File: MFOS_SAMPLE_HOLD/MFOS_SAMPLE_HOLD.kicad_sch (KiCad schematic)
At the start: 94 parts, among them J1 Jack-DC, J10 Conn_01x01, J11 Conn_01x01, J12 Conn_01x01, J13 Conn_01x01, J14 Conn_01x01, J15 Conn_01x01, J16 Conn_01x01, J17 Conn_01x01, J18 Conn_01x01, J19 Conn_01x01, J2 Jack-DC, J20 Conn_01x01, J3 Jack-DC, J4 Jack-DC, J5 Jack-DC, J6 Jack-DC, J7 Jack-DC, J8 Conn_01x01, J9 Conn_01x01, Q1 2N3904, Q2 2N3904, Q3 2N3904, Q4 J112, Q5 J112, Q6 J112, U1 TL074, U2 TL082, U3 LF444

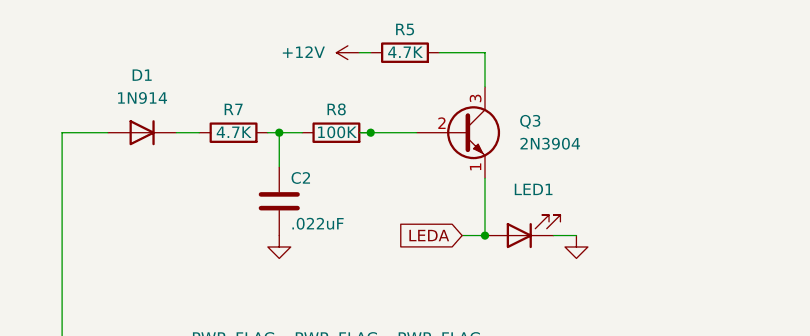
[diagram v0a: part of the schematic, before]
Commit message: Updated BOM, renamed VCO > MFOS_VCO
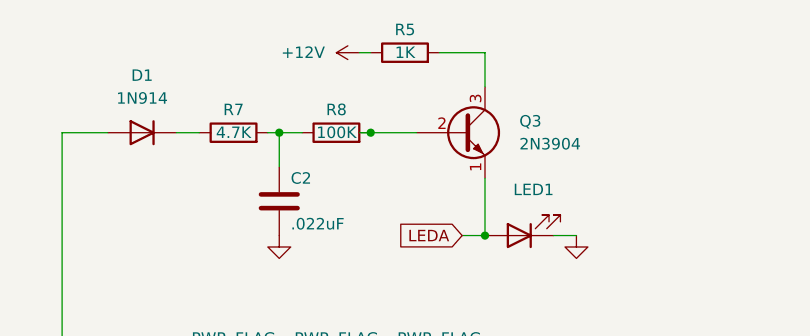
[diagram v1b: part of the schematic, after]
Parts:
- R5: value 4.7K -> 1K
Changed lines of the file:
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@@
     (in_bom yes) (on_board yes)
     (property "Reference" "R5" (id 0) (at 198.12 24.13 90))
-    (property "Value" "4.7K" (id 1) (at 198.12 26.67 90))
+    (property "Value" "1K" (id 1) (at 198.12 26.67 90))
     (property "Footprint" "" (id 2) (at 198.12 28.448 90)
       (effects (font (size 1.27 1.27)) hide)
@@
     )
     (path "/9da687fc-1551-41db-960a-e23aea2daa27"
-      (reference "R5") (unit 1) (value "4.7K") (footprint "")
+      (reference "R5") (unit 1) (value "1K") (footprint "")
     )
     (path "/f7d900a7-907c-49dd-9ace-fc968800f1a3"

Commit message: Reviewed BOM
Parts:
- C17: symbol Device:C -> dhk:C_Polystyrene
- J10, J11, J12, J13, J14, J15, J16, J17, J18, J19, J20, J8, J9: now left out of the parts list

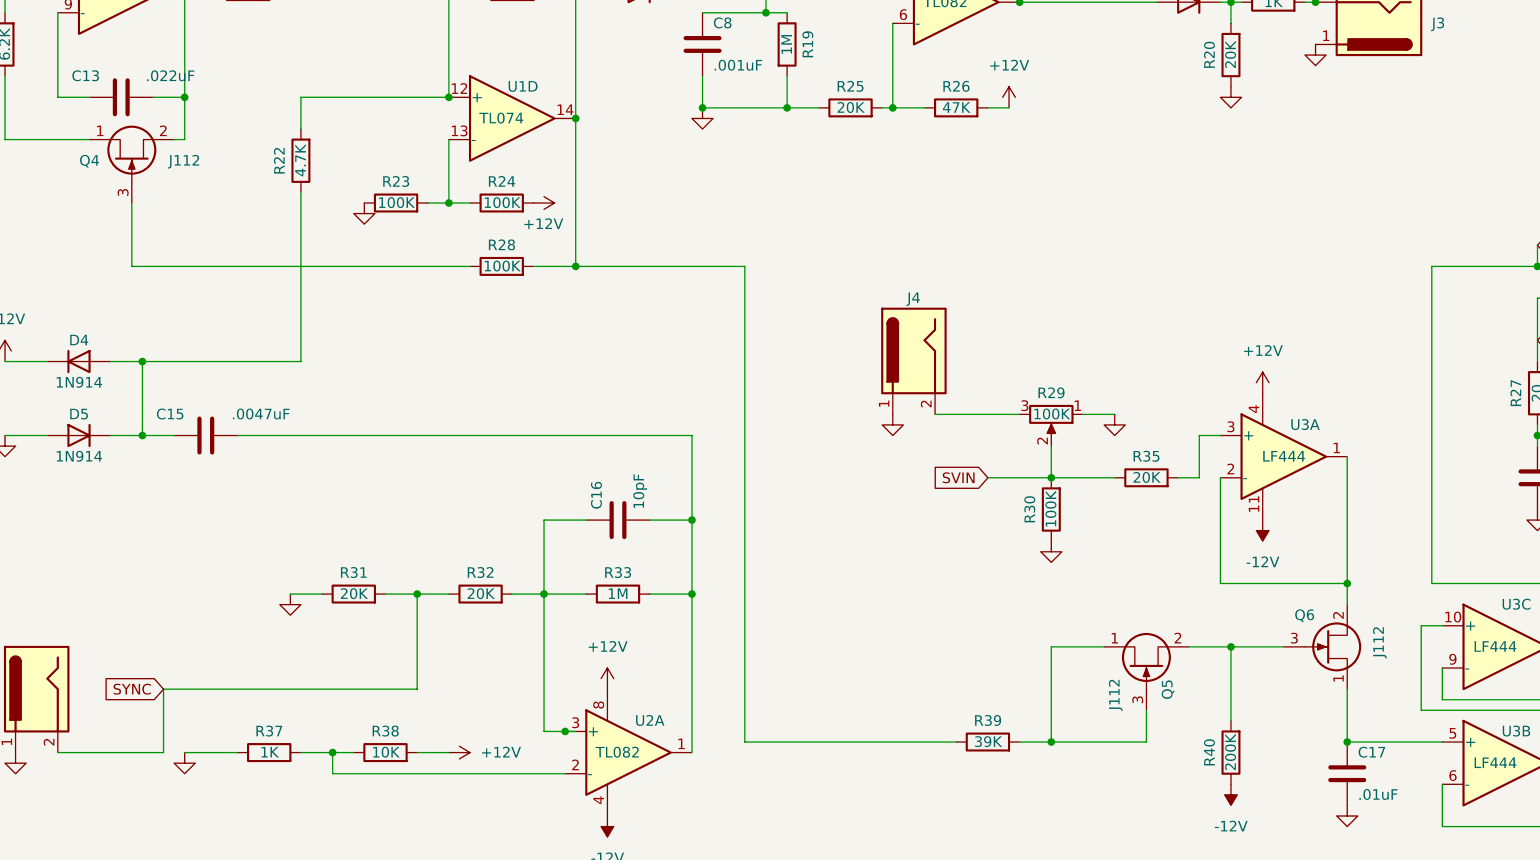
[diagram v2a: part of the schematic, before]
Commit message: Designs adapted for BOM
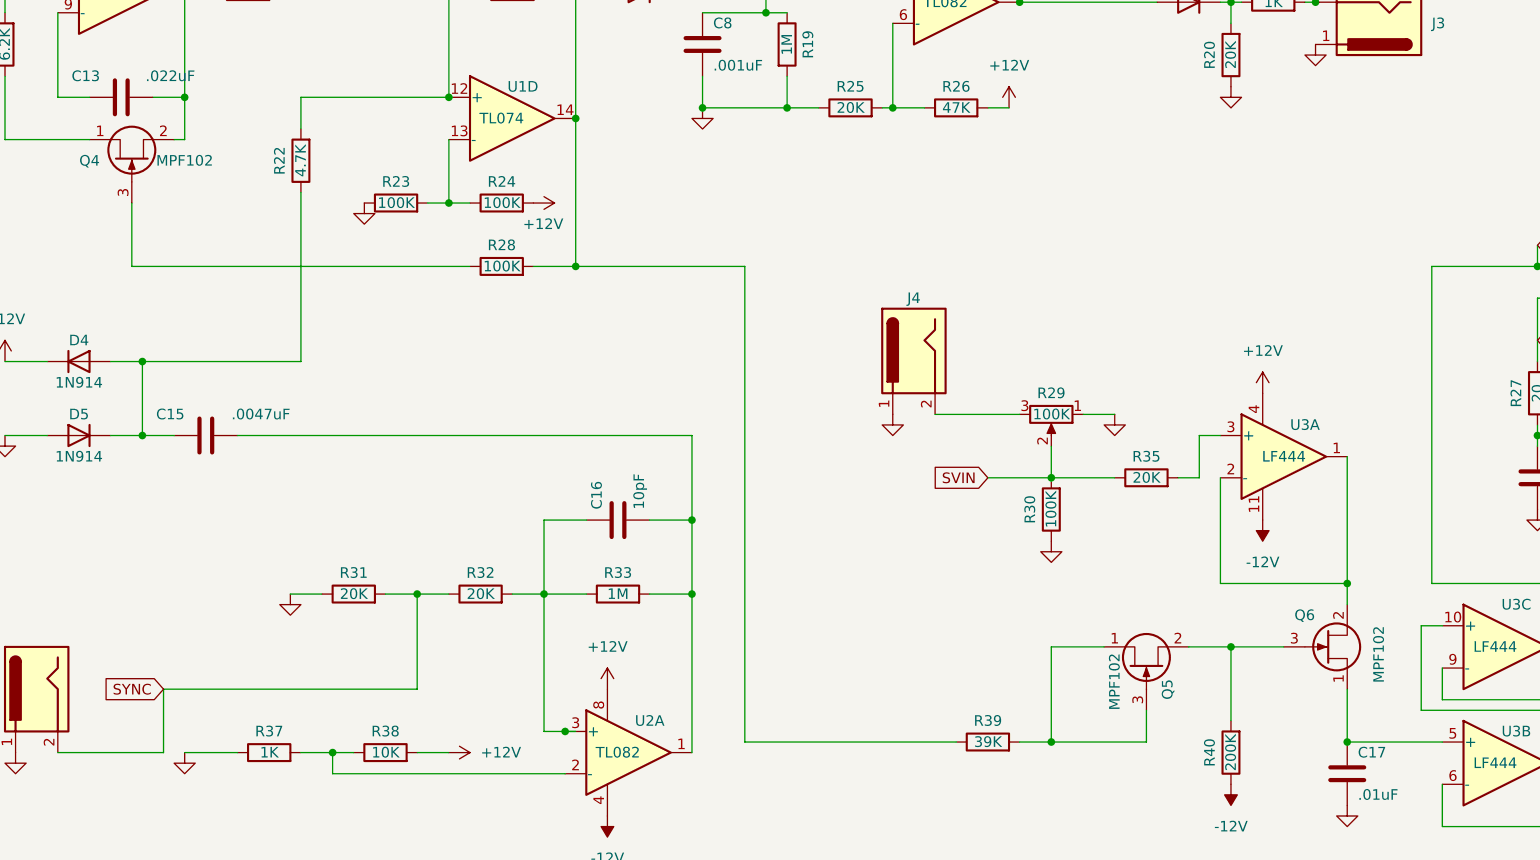
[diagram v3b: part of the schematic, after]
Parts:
- Q4, Q5, Q6: value J112 -> MPF102
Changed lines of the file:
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@@
       (effects (font (size 1.27 1.27)) (justify left))
     )
-    (property "Value" "J112" (id 1) (at 163.83 181.61 0)
+    (property "Value" "MPF102" (id 1) (at 163.83 181.61 0)
       (effects (font (size 1.27 1.27)) (justify left))
     )
@@
     (in_bom yes) (on_board yes)
     (property "Reference" "Q4" (id 0) (at 40.64 115.57 90))
-    (property "Value" "J112" (id 1) (at 52.07 115.57 90))
+    (property "Value" "MPF102" (id 1) (at 52.07 115.57 90))
     (property "Footprint" "" (id 2) (at 47.625 110.49 0)
       (effects (font (size 1.27 1.27) italic) (justify left) hide)
@@
       (effects (font (size 1.27 1.27)) (justify left))
     )
-    (property "Value" "J112" (id 1) (at 195.58 171.45 90)
+    (property "Value" "MPF102" (id 1) (at 195.58 171.45 90)
       (effects (font (size 1.27 1.27)) (justify left))
     )
@@
     )
     (path "/7319e780-225d-49c8-b443-e4647f2dcf5f"
-      (reference "Q4") (unit 1) (value "J112") (footprint "")
+      (reference "Q4") (unit 1) (value "MPF102") (footprint "")
     )
     (path "/411993a9-df9b-475b-acd7-b390e54f2b94"
-      (reference "Q5") (unit 1) (value "J112") (footprint "")
+      (reference "Q5") (unit 1) (value "MPF102") (footprint "")
     )
     (path "/945ed899-8bd2-4078-9704-4e2d00c36e55"
-      (reference "Q6") (unit 1) (value "J112") (footprint "")
+      (reference "Q6") (unit 1) (value "MPF102") (footprint "")
     )
     (path "/e2538d12-72dc-4511-9398-0137f338d898"
